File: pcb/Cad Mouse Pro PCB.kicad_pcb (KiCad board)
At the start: 2 copper layers, 69.8 x 69.8 mm, 18 parts, among them J1 Conn_01x12_Pin, J2 Conn_01x12_Pin

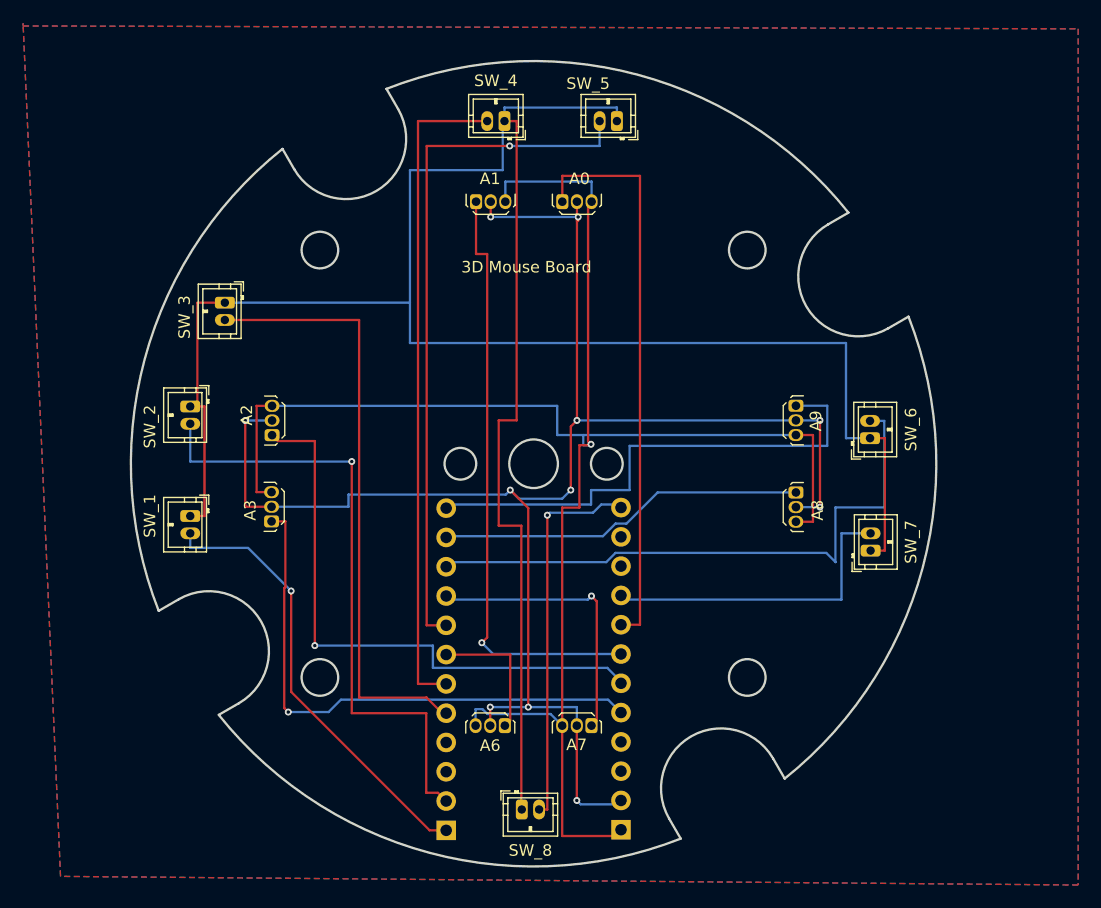
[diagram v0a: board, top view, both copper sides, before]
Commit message: Added pro micro submodul and connectors for debugging
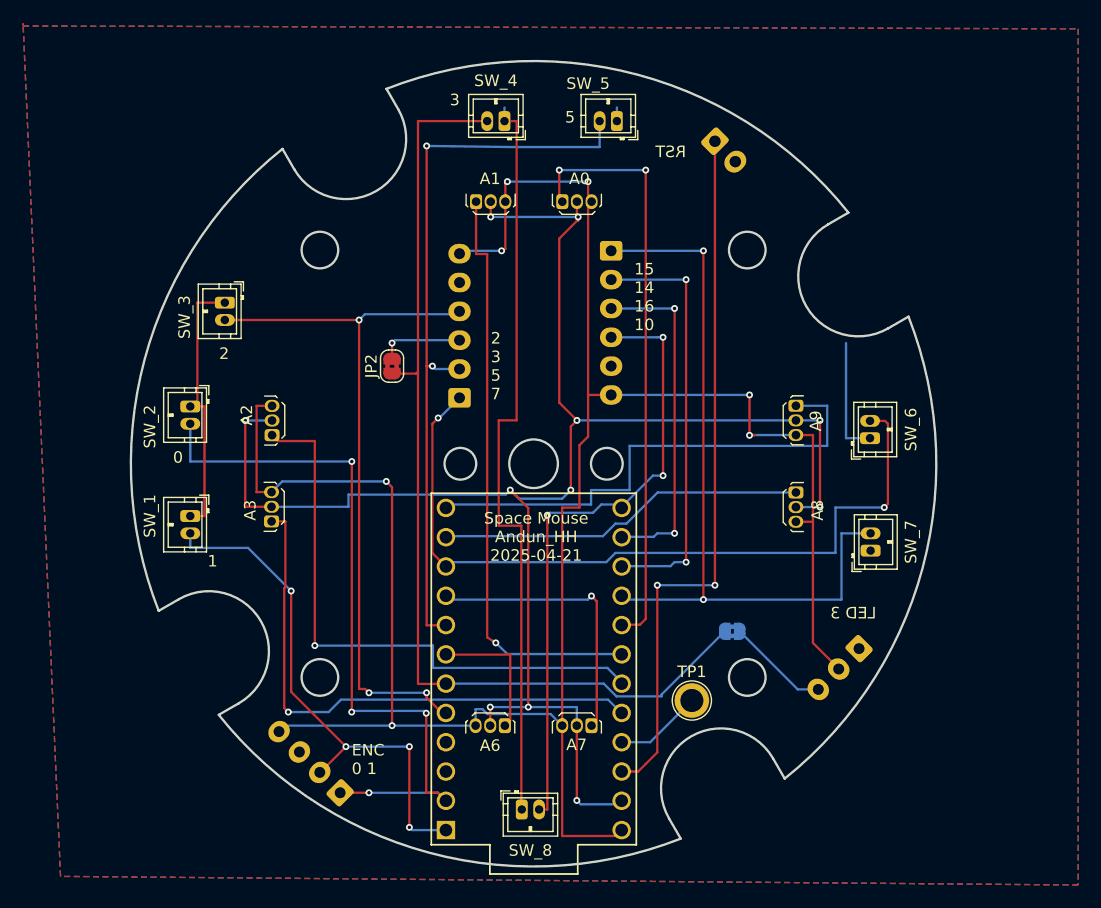
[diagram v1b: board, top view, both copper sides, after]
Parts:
- added J3: Key2, Connector_JST:JST_XH_S6B-XH-A-1_1x06_P2.50mm_Horizontal, B.Cu at (137.0, 69.5)
- added J4: Key1, Connector_JST:JST_XH_S6B-XH-A-1_1x06_P2.50mm_Horizontal, B.Cu at (123.8, 82.2)
- added J5: LED, Connector_JST:JST_XH_S3B-XH-A-1_1x03_P2.50mm_Horizontal, B.Cu at (158.5, 104.0)
- added JP1: SolderJumper_2_Bridged, Jumper:SolderJumper-2_P1.3mm_Bridged2Bar_RoundedPad1.0x1.5mm, B.Cu at (147.5, 102.5)
- added JP2: SolderJumper_2_Bridged, Jumper:SolderJumper-2_P1.3mm_Bridged2Bar_RoundedPad1.0x1.5mm, F.Cu at (118.0, 79.5)
- added TP1: TestPoint, TestPoint:TestPoint_Plated_Hole_D2.0mm, F.Cu at (144.0, 108.5)
- added U1: ProMicro, promicro:ProMicro, B.Cu at (130.3, 105.8)
- J1: value Conn_01x12_Pin -> reset; footprint Connector_PinHeader_2.54mm:PinHeader_1x12_P2.54mm_Vertical -> Connector_JST:JST_XH_S2B-XH-A-1_1x02_P2.50mm_Horizontal
- J2: value Conn_01x12_Pin -> encoder; footprint Connector_PinHeader_2.54mm:PinHeader_1x12_P2.54mm_Vertical -> Connector_JST:JST_XH_S4B-XH-A-1_1x04_P2.50mm_Horizontal
- moved J1 64.1 mm to (146.0, 60.0), turned to -45 degrees
- moved J2 24.6 mm to (113.5, 116.5), turned to 135 degrees
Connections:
- A0 pad 1: Net-(J2-Pin_8) -> /A0
- A0 pad 3: Net-(J2-Pin_1) -> VCC
- A1 pad 1: Net-(J2-Pin_7) -> /A1
- A1 pad 3: Net-(J2-Pin_1) -> VCC
- A2 pad 1: Net-(J2-Pin_6) -> /A2
- A2 pad 3: Net-(J2-Pin_1) -> VCC
- A3 pad 1: Net-(J2-Pin_5) -> /A3
- A3 pad 3: Net-(J2-Pin_1) -> VCC
- A6 pad 1: Net-(J1-Pin_7) -> /A6
- A6 pad 3: Net-(J2-Pin_1) -> VCC
- A7 pad 1: Net-(J1-Pin_9) -> /A7
- A7 pad 3: Net-(J2-Pin_1) -> VCC
- A8 pad 1: Net-(J1-Pin_11) -> /A8
- A8 pad 3: Net-(J2-Pin_1) -> VCC
- A9 pad 1: Net-(J1-Pin_12) -> /A9
- A9 pad 3: Net-(J2-Pin_1) -> VCC
- J1 pad 1: Net-(J1-Pin_1) -> /RST
- J1 pad 2: Net-(J1-Pin_2) -> GND
- J2 pad 1: Net-(J2-Pin_1) -> /P0
- J2 pad 2: GND -> /P1
- J2 pad 3: unconnected-(J2-Pin_3-Pad3) -> GND
- J2 pad 4: unconnected-(J2-Pin_4-Pad4) -> VCC
- SW_1 pad 1: Net-(SW_1-Pin_1) -> GND
- SW_1 pad 2: Net-(J1-Pin_1) -> /P1
- SW_2 pad 1: Net-(SW_1-Pin_1) -> GND
- SW_2 pad 2: Net-(J1-Pin_2) -> /P0
- SW_3 pad 1: Net-(SW_1-Pin_1) -> GND
- SW_3 pad 2: Net-(J1-Pin_5) -> /P2
- SW_4 pad 1: Net-(SW_1-Pin_1) -> GND
- SW_4 pad 2: Net-(J1-Pin_6) -> /P3
- SW_5 pad 1: Net-(SW_1-Pin_1) -> GND
- SW_5 pad 2: Net-(J1-Pin_8) -> /P5
- SW_6 pad 1: Net-(SW_1-Pin_1) -> GND
- SW_6 pad 2: Net-(J1-Pin_10) -> /P7
- SW_7 pad 1: Net-(SW_1-Pin_1) -> GND
- SW_7 pad 2: Net-(J2-Pin_9) -> /P15
- SW_8 pad 1: Net-(SW_1-Pin_1) -> GND
- SW_8 pad 2: Net-(J2-Pin_12) -> /P10
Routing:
- net Net-(SW_1-Pin_1): track 203.7 -> 0.00 mm
- net VCC: track 0.00 -> 196.2 mm, vias 0 -> 7
- net Net-(J2-Pin_1): track 153.9 -> 0.00 mm, vias 1 -> 0
- net GND: track 145.9 -> 247.7 mm
- net /P3: track 0.00 -> 86.6 mm
- net /P7: track 0.00 -> 67.9 mm, vias 0 -> 2
- net /P15: track 0.00 -> 65.8 mm, vias 0 -> 2
- net /P0: track 0.00 -> 64.2 mm, vias 0 -> 4
- net /P5: track 0.00 -> 63.5 mm, vias 0 -> 2
- net /RST: track 0.00 -> 61.8 mm, vias 0 -> 2
- net /P2: track 0.00 -> 61.7 mm, vias 0 -> 3
- net Net-(J1-Pin_8): track 60.4 -> 0.00 mm, vias 1 -> 0
- net Net-(J1-Pin_6): track 57.3 -> 0.00 mm
- net Net-(J1-Pin_2): track 54.5 -> 0.00 mm, vias 1 -> 0
- net /P10: track 0.00 -> 54.4 mm, vias 0 -> 3
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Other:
- board text added: "0"
- board text added: "1"
- board text added: "15 14 16 10"
- board text added: "2"
- board text added: "2 3 5 7"
- board text added: "3"
- board text added: "5"
- board text added: "ENC 0 1"
- board text added: "LED 3"
- board text added: "RST"
- board text added: "Space Mouse Andun_HH 2025-04-21"
- board text removed: "3D Mouse Board"
